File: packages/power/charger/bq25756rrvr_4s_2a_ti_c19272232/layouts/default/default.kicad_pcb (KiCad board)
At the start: 2 copper layers, 29 parts

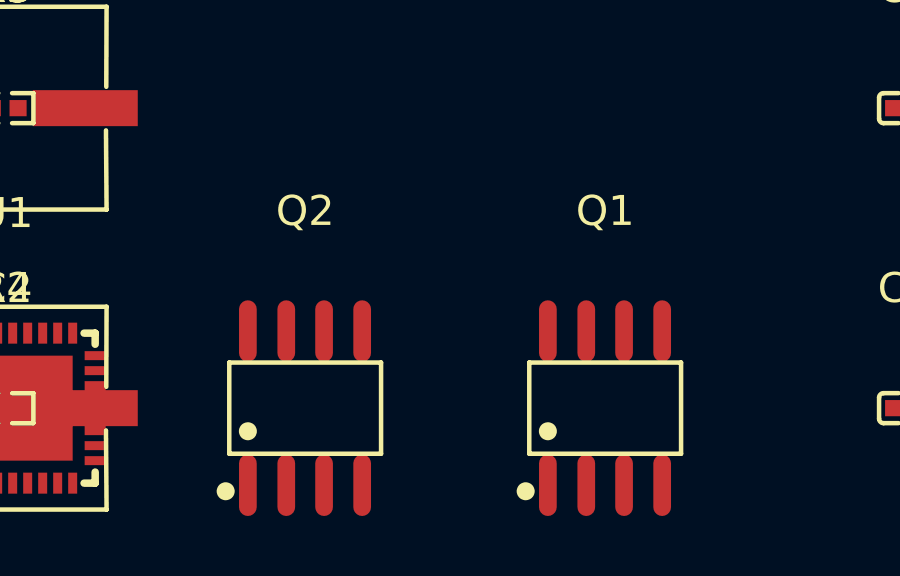
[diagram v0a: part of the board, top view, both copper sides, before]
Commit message: Switch BQ25756 charger to Vishay dual MOSFETs
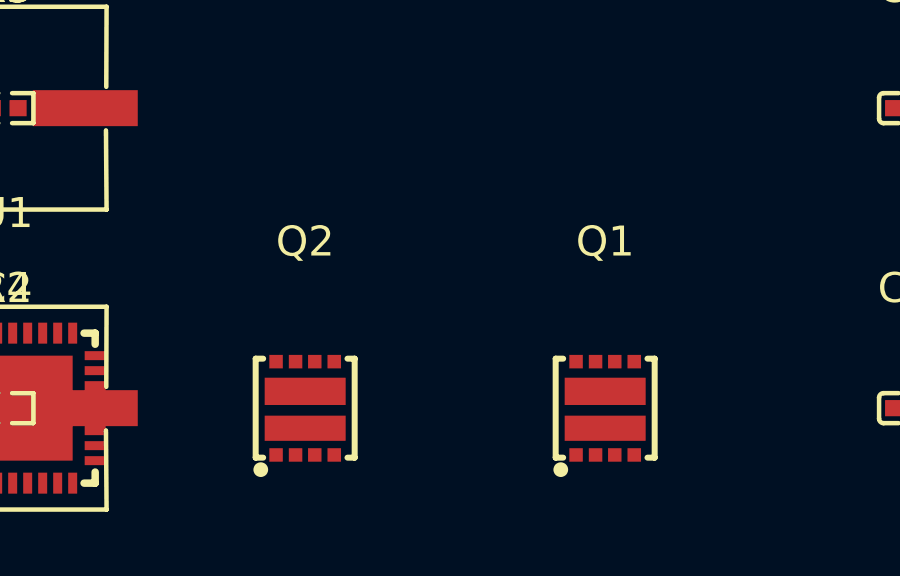
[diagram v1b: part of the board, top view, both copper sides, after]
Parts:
- Q1, Q2: footprint Texas_Instruments_CSD88537ND:SOIC-8_L4.9-W3.9-P1.27-LS6.0-BL -> Vishay_Intertech_SIZ250DT_T1_GE3:POWERPAIR-8_L3.3-W3.3-P0.65-BL_SIZ260DT-T1-GE3
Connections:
- Q1 pad 1: bootstrap_2-power-lv -> vac_bypass-power-lv
- Q1 pad 2: 19 -> vac_bypass-power-lv
- Q1 pad 5: bootstrap_2-power-lv -> battery_bypass-power-hv
- Q1 pad 6: bootstrap_2-power-lv -> battery_bypass-power-hv
- Q1 pad 8: battery_bypass-power-hv -> 1
- Q2 pad 1: bootstrap_1-power-lv -> vac_bypass-power-lv
- Q2 pad 2: 2 -> vac_bypass-power-lv
- Q2 pad 5: bootstrap_1-power-lv -> vac_bypass-power-hv
- Q2 pad 6: bootstrap_1-power-lv -> vac_bypass-power-hv
- Q2 pad 8: vac_bypass-power-hv -> 1-1
- U1 pad 19: 19 -> 1
- U1 pad 27: 2 -> 1-1

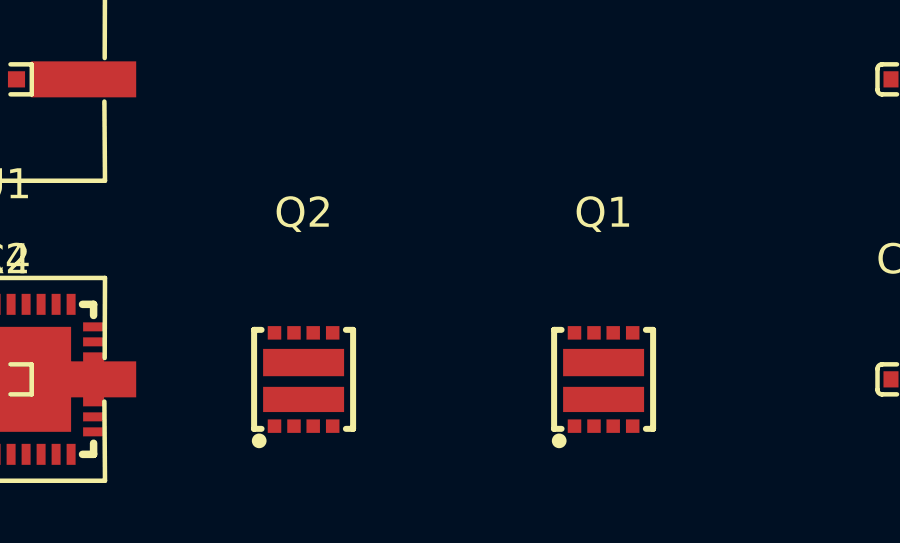
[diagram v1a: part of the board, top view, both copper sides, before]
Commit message: Switch BQ25756 charger to XRS30V06D
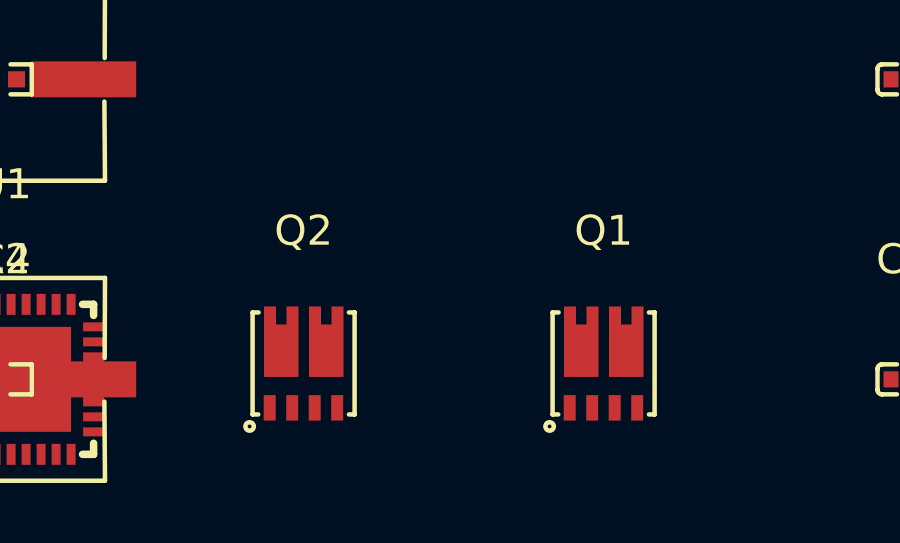
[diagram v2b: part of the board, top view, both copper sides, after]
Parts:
- Q1, Q2: footprint Vishay_Intertech_SIZ250DT_T1_GE3:POWERPAIR-8_L3.3-W3.3-P0.65-BL_SIZ260DT-T1-GE3 -> XNRUSEMI_XRS30V06D:DFN-8_L3.3-W3.3-P0.75-TL
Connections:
- Q1 pad 1: vac_bypass-power-lv -> bootstrap_2-power-lv
- Q1 pad 2: vac_bypass-power-lv -> 19
- Q1 pad 5: battery_bypass-power-hv -> bootstrap_2-power-lv
- Q1 pad 8: 1 -> battery_bypass-power-hv
- Q2 pad 1: vac_bypass-power-lv -> bootstrap_1-power-lv
- Q2 pad 2: vac_bypass-power-lv -> 2
- Q2 pad 5: vac_bypass-power-hv -> bootstrap_1-power-lv
- Q2 pad 8: 1-1 -> vac_bypass-power-hv
- U1 pad 19: 1 -> 19
- U1 pad 27: 1-1 -> 2
